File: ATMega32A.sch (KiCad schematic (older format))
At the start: 21 parts, among them J201 AVR-ISP-6, J202 UART, U201 ATmega32A-AU, Y201 16MHz

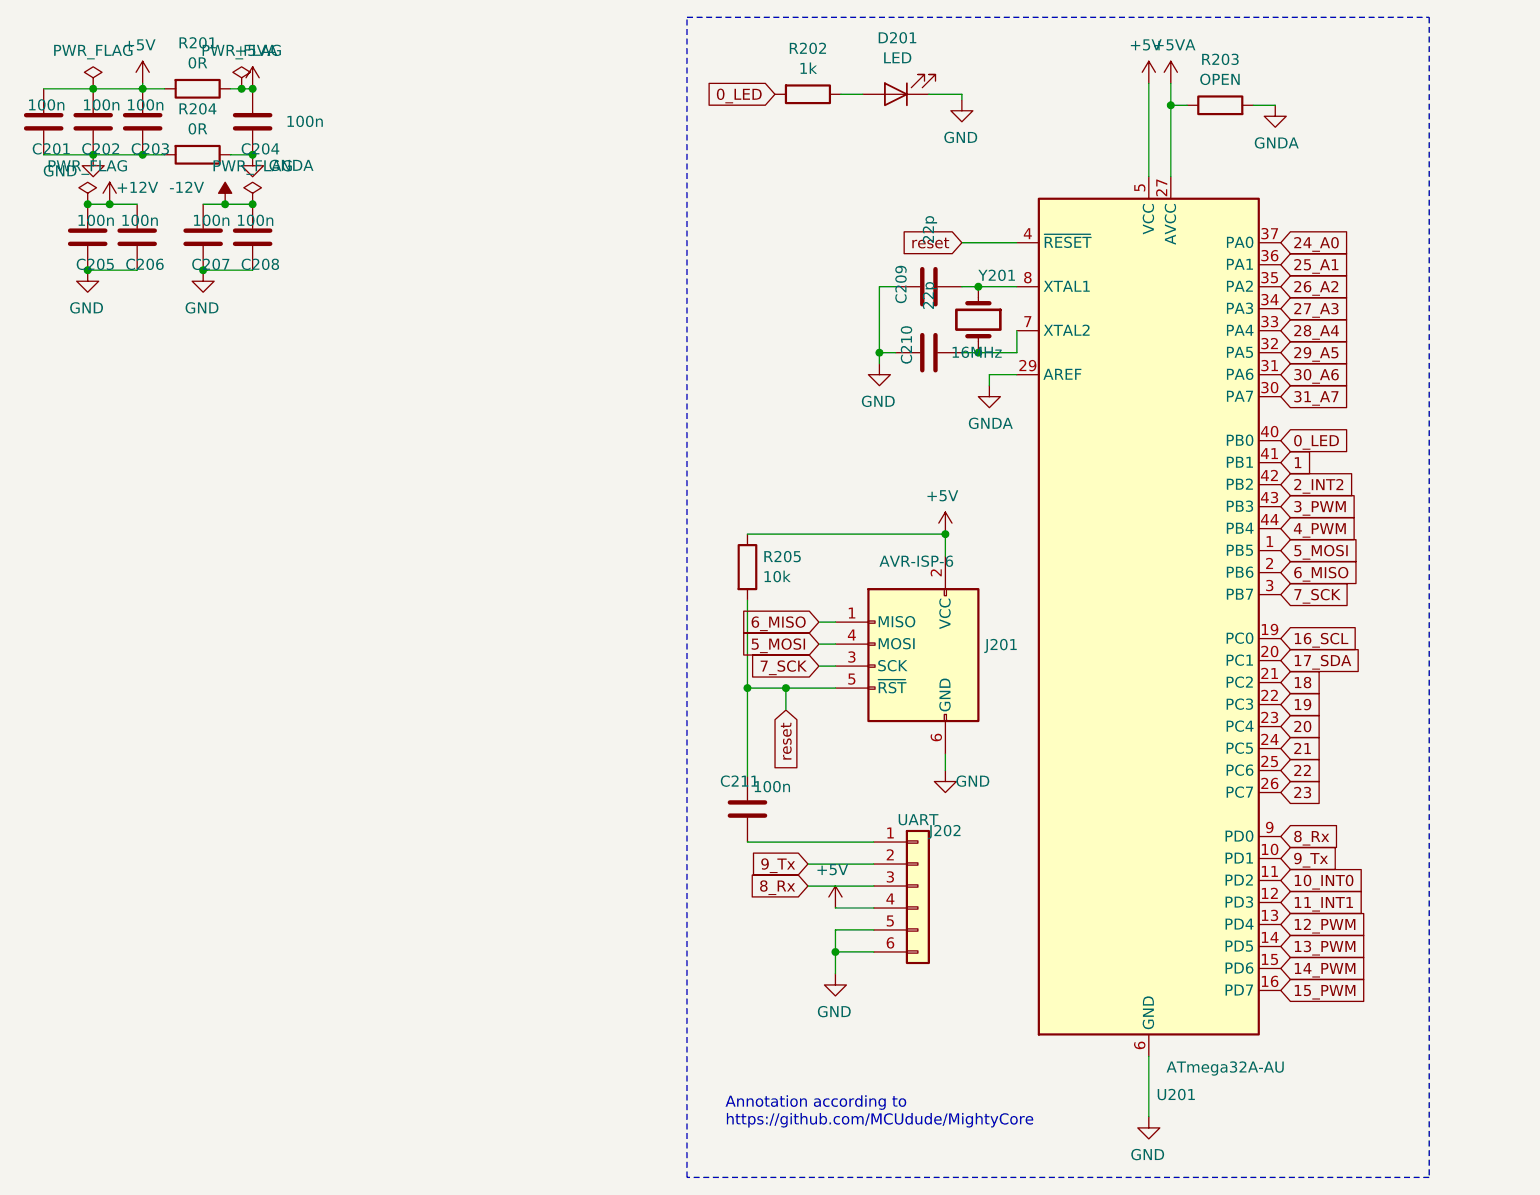
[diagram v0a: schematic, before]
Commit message: Hierarchical ATMega32 pins
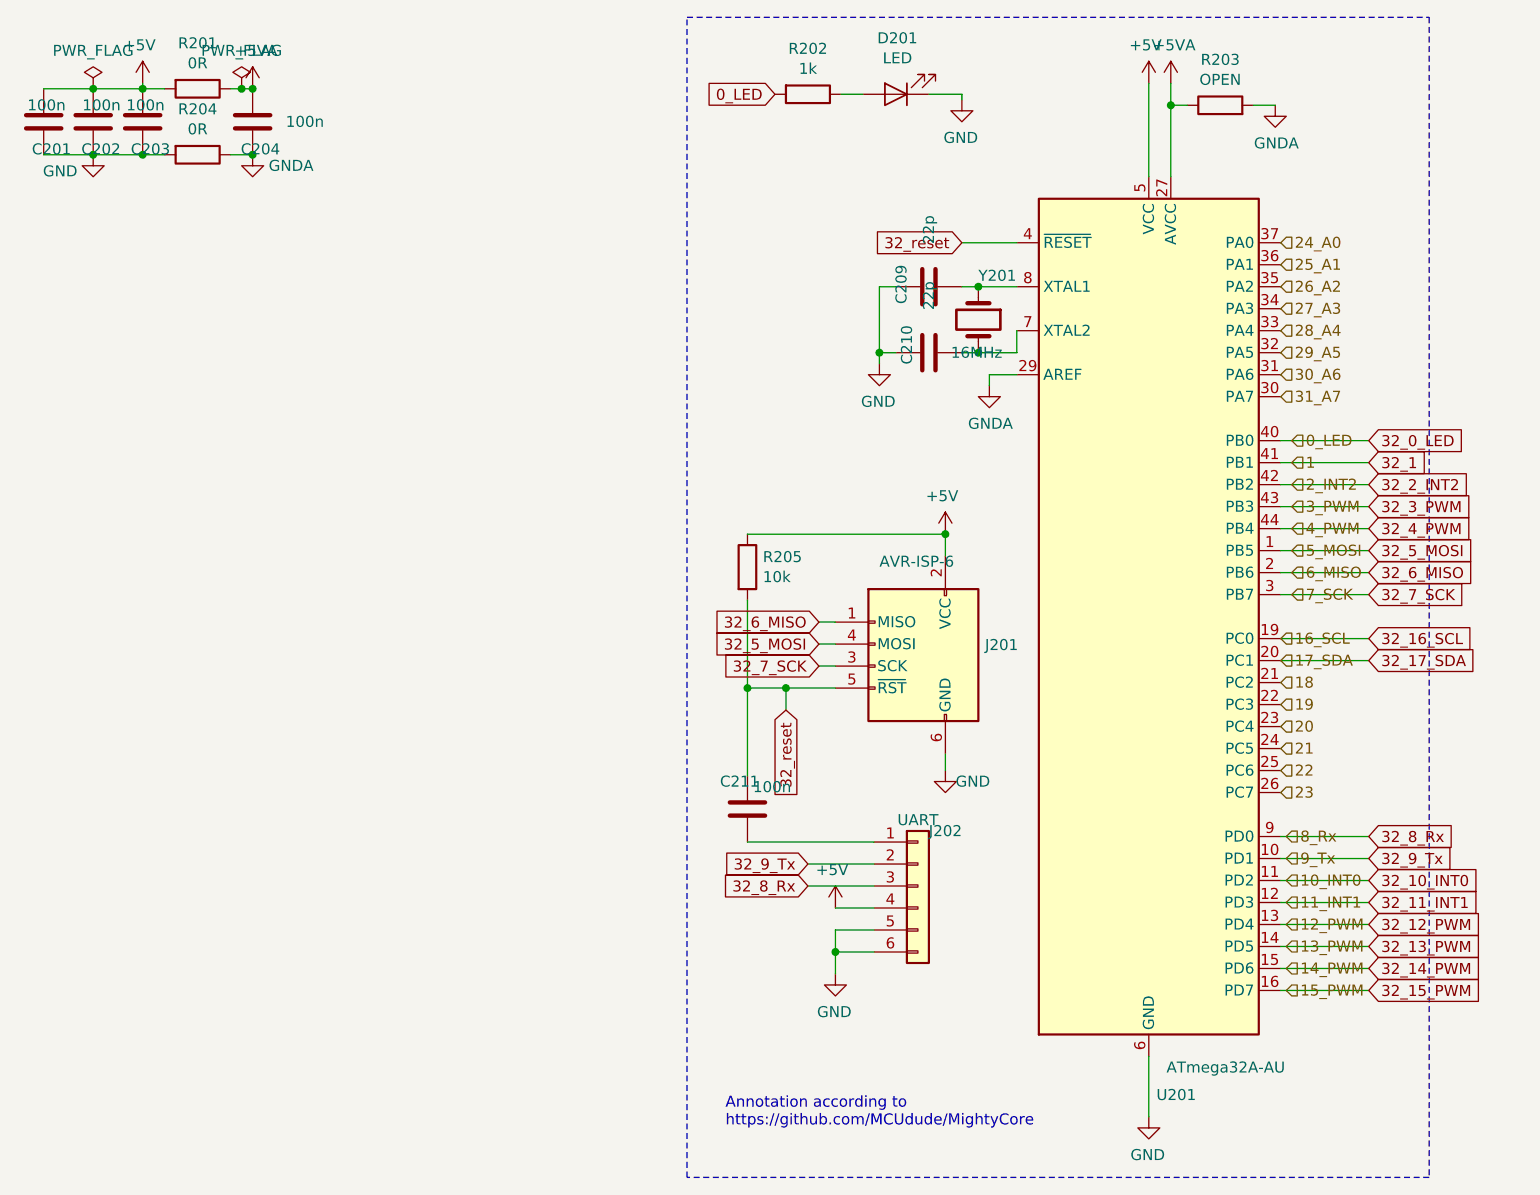
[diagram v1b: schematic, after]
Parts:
- removed C205, C207: 100n, Capacitor_SMD:C_1206_3216Metric_Pad1.42x1.75mm_HandSolder, symbol Device:C
- removed C206, C208: 100n, Capacitor_SMD:C_0805_2012Metric_Pad1.15x1.40mm_HandSolder, symbol Device:C
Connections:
- net 1 renamed 32_1
- net 10_INT0 renamed 32_10_INT0
- net 11_INT1 renamed 32_11_INT1
- net 12_PWM renamed 32_12_PWM
- net 13_PWM renamed 32_13_PWM
- net 14_PWM renamed 32_14_PWM
- net 15_PWM renamed 32_15_PWM
- net 16_SCL renamed 32_16_SCL
- net 17_SDA renamed 32_17_SDA
- net 2_INT2 renamed 32_2_INT2
- net 3_PWM renamed 32_3_PWM
- net 4_PWM renamed 32_4_PWM
- net 5_MOSI renamed 32_5_MOSI
- net 6_MISO renamed 32_6_MISO
- net 7_SCK renamed 32_7_SCK
- net 8_Rx renamed 32_8_Rx
- net 9_Tx renamed 32_9_Tx
- net reset renamed 32_reset

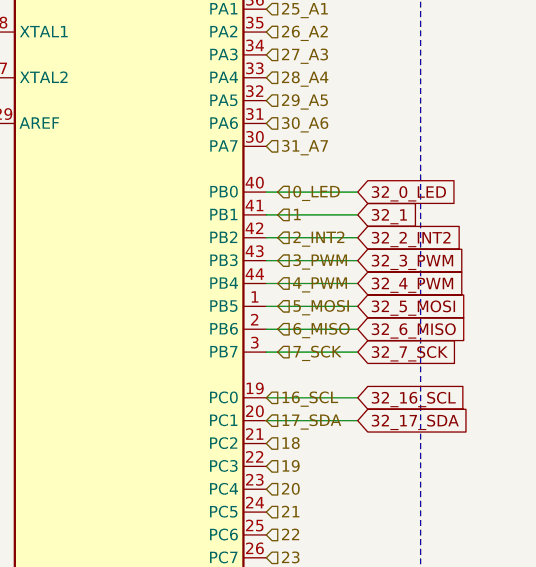
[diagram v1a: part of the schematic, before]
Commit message: 2x Sallen Key LP out from DAC
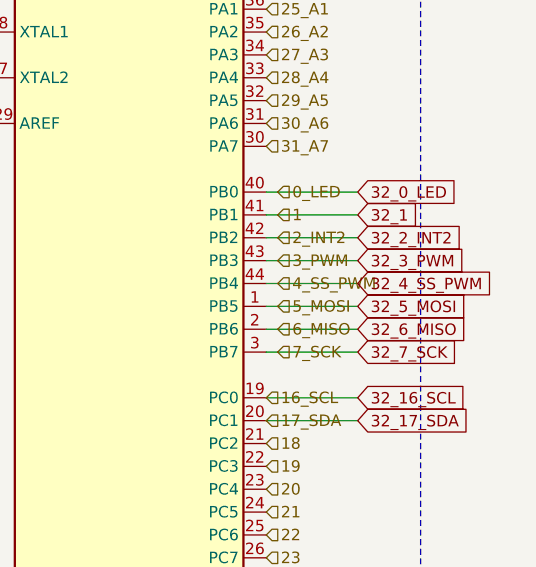
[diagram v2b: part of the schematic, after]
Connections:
- net 32_4_PWM renamed 32_4_SS_PWM
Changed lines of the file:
@@
 32_3_PWM
 Text GLabel 7250 3300 2    50   Input ~ 0
-32_4_PWM
+32_4_SS_PWM
 Text GLabel 7250 3400 2    50   Input ~ 0
 32_5_MOSI
@@
 3_PWM
 Text HLabel 6900 3300 2    50   Input ~ 0
-4_PWM
+4_SS_PWM
 Text HLabel 6900 3400 2    50   Input ~ 0
 5_MOSI

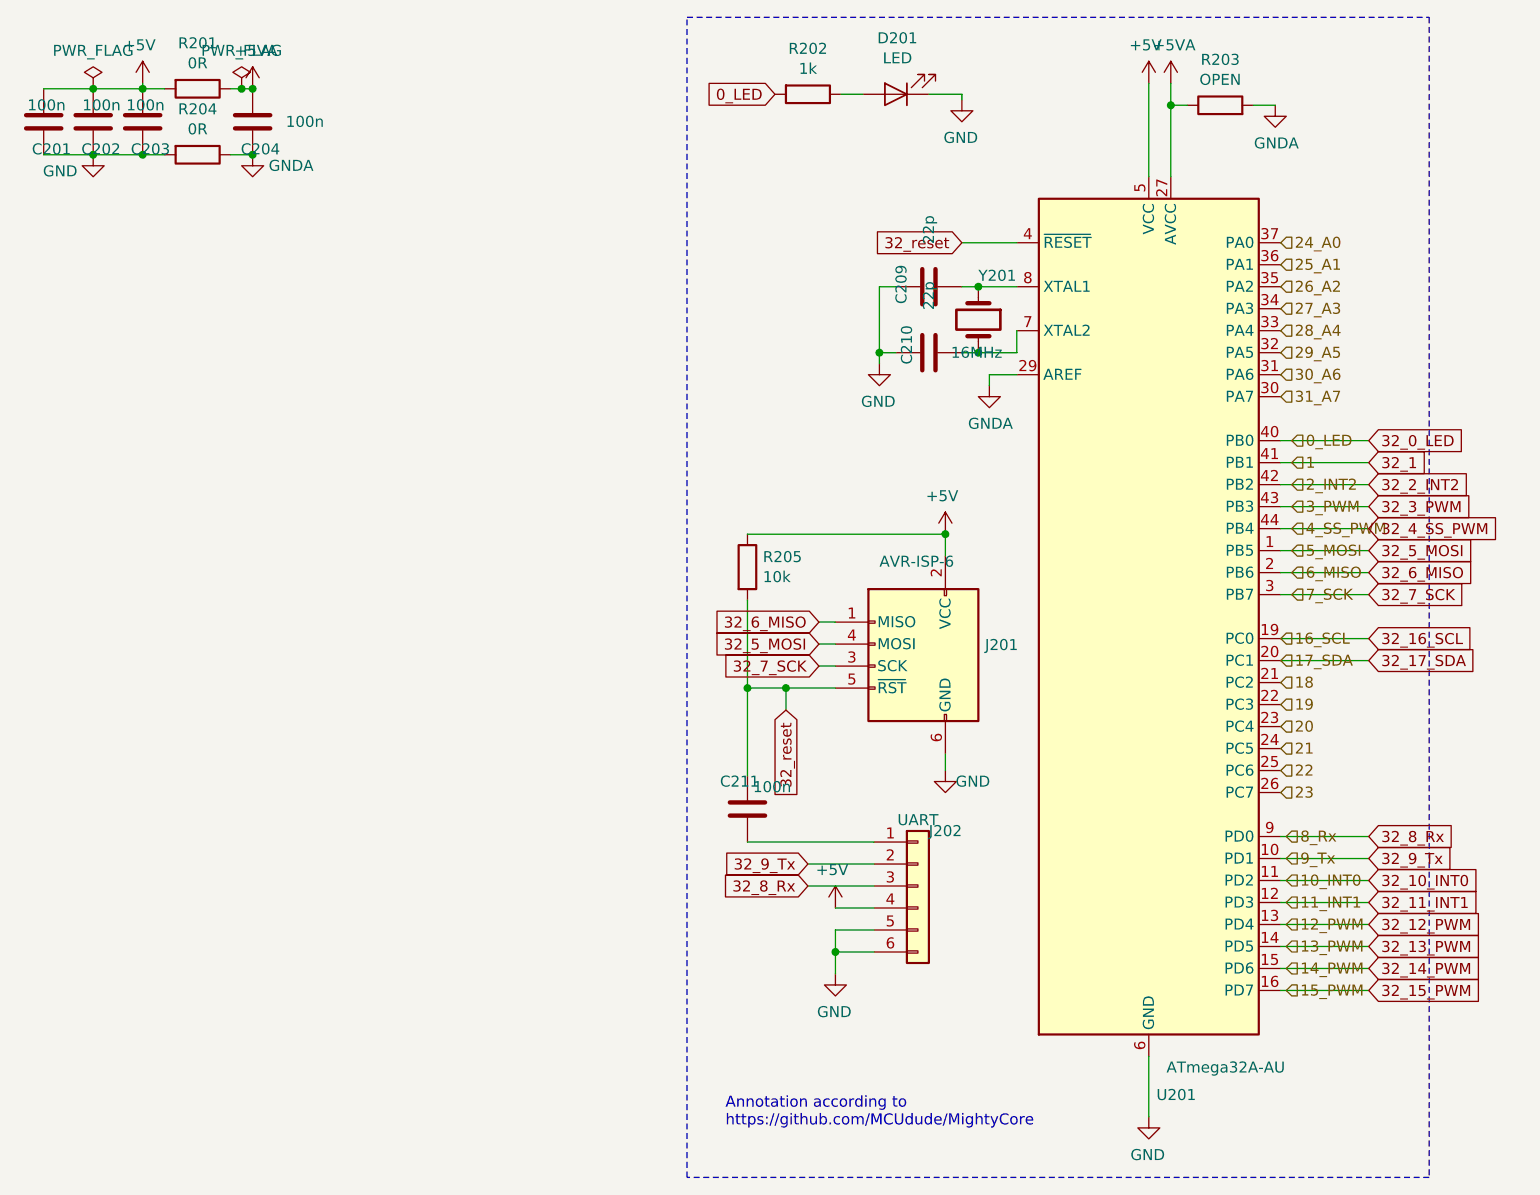
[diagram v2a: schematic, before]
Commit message: Dual uP hierarchy
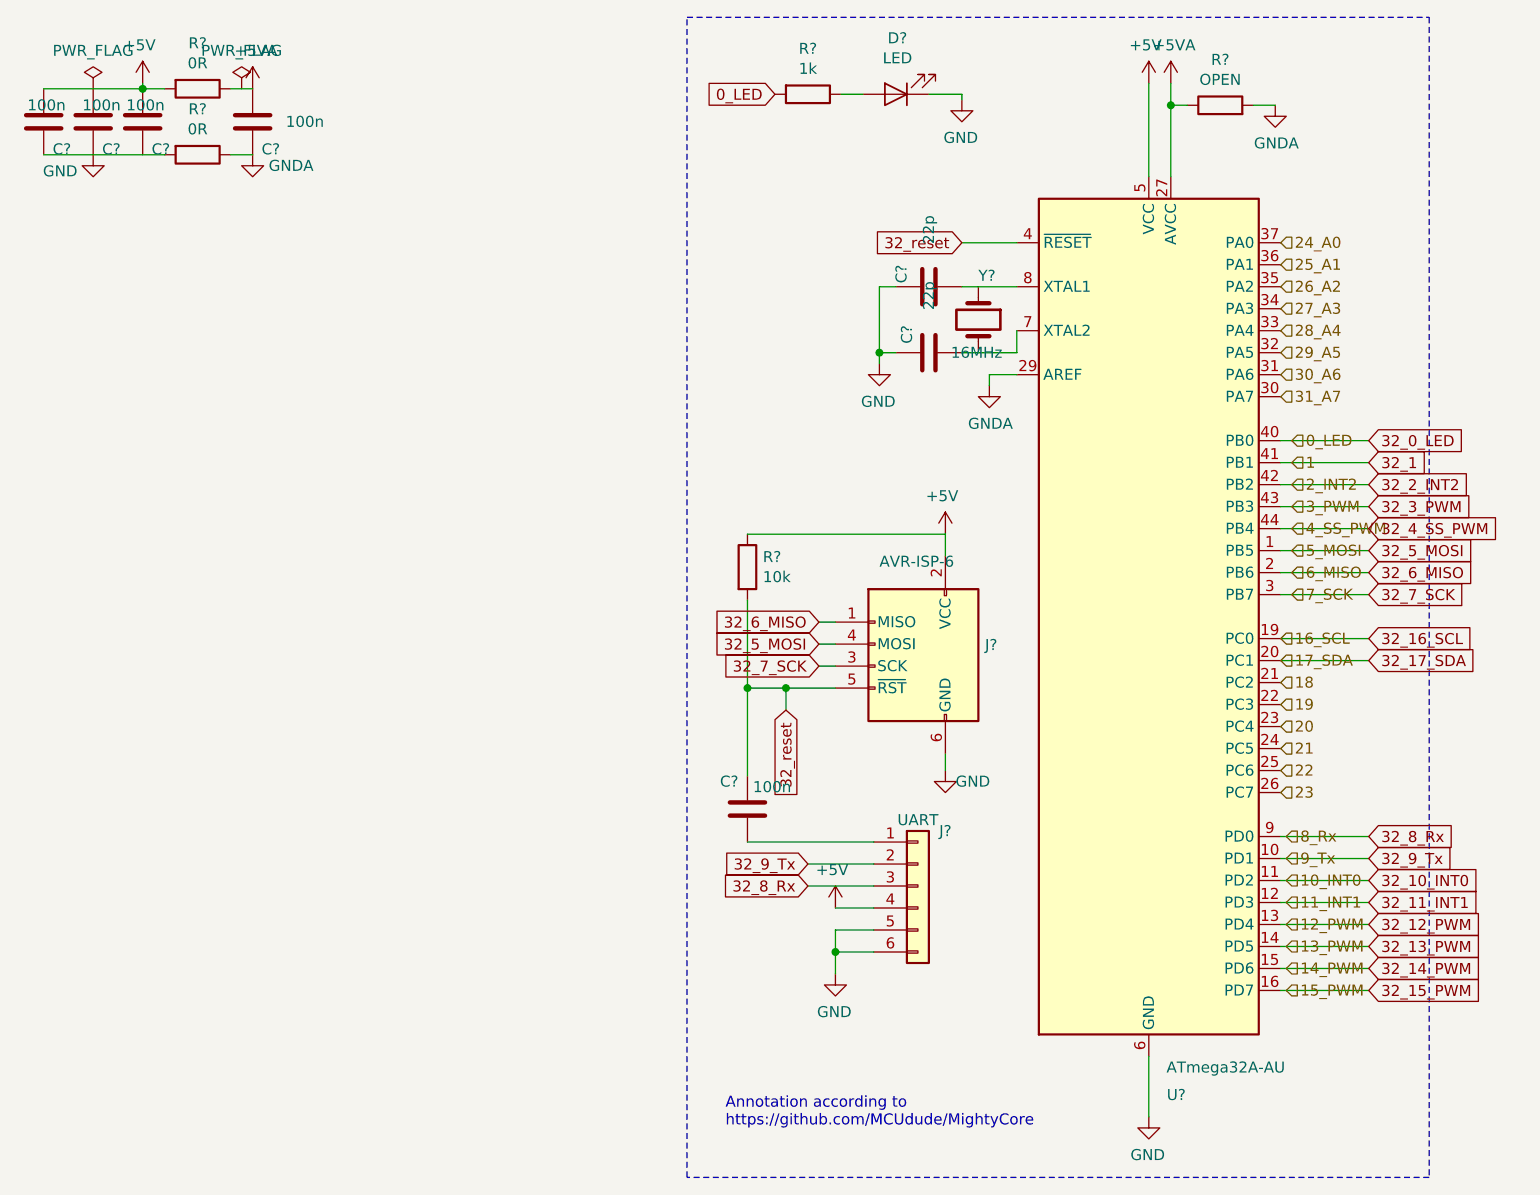
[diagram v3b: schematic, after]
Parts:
- renumbered C209 to C205, C210 to C206, C211 to C207
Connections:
- net +5V: no longer C202.2
- net GND: no longer C201.1, C203.1, R204.2
- net at C206.1, U201.7 (XTAL2): no longer Y201.2
- net at C205.1, U201.8 (XTAL1): no longer Y201.1
- new net: C201.1, R204.2
